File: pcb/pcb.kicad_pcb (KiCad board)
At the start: 2 copper layers, 54 parts, among them K00 Kailh Choc, K01 Kailh Choc, K02 Kailh Choc, K03 Kailh Choc, K10 Kailh Choc, K11 Kailh Choc, K12 Kailh Choc, K13 Kailh Choc, K20 Kailh Choc, K21 Kailh Choc, K22 Kailh Choc, K23 Kailh Choc, K30 Kailh Choc, K31 Kailh Choc, K32 Kailh Choc, K33 Kailh Choc, K40 Kailh Choc, K41 Kailh Choc, K42 Kailh Choc, K43 Kailh Choc, K50 Kailh Choc, K51 Kailh Choc, K52 Kailh Choc, K53 Kailh Choc, K60 Kailh Choc, K61 Kailh Choc, SW1 SW_DPST, U1 nice_nano

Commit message: first pass at pcb and case
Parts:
- removed D00, D01, D02, D03, D10, D11, D12, D13, D20, D21, D22, D23, D30, D31, D32, D33, D40, D41, D42, D43, D50, D51, D52, D53, D60, D61: 1N4148, Diode_THT:D_DO-35_SOD27_P7.62mm_Horizontal
- added J1: Screw_Terminal_01x02, Connector_JST:JST_PH_S2B-PH-K_1x02_P2.00mm_Horizontal, F.Cu at (189.5, 99.1)
- SW1: moved to B.Cu
- moved K13 336.6 mm to (90.8, 80.4), turned to 10.6 degrees
- moved K03 316.9 mm to (73.4, 85.4), turned to 10.6 degrees
- moved K00 304.1 mm to (82.8, 135.6), turned to 10.6 degrees
- moved K22 297.8 mm to (112.4, 88.3), turned to 8.36 degrees
- moved K33 294.9 mm to (131.7, 66.0), turned to 4.47 degrees
- moved K41 292.2 mm to (154.6, 100.4)
- moved K01 286.7 mm to (79.7, 118.8), turned to 10.6 degrees
- moved K10 286.6 mm to (100.2, 130.6), turned to 10.6 degrees
- moved K32 272.9 mm to (133.0, 83.0), turned to 4.47 degrees
- moved K11 269.7 mm to (97.1, 113.8), turned to 10.6 degrees
- moved K02 269.6 mm to (76.6, 102.1), turned to 10.6 degrees
- moved K43 257.2 mm to (154.6, 66.4)
- moved K51 254.7 mm to (172.6, 102.1)
- moved K12 253.1 mm to (93.9, 97.1), turned to 10.6 degrees
- moved K30 252.3 mm to (135.7, 116.9), turned to 4.47 degrees
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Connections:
- K00 pad 2: Net-(D00-Pad2) -> Row0
- K01 pad 2: Net-(D01-Pad2) -> Row1
- K02 pad 2: Net-(D02-Pad2) -> Row2
- K03 pad 2: Net-(D03-Pad2) -> Row3
- K10 pad 2: Net-(D10-Pad2) -> Row0
- K11 pad 2: Net-(D11-Pad2) -> Row1
- K12 pad 2: Net-(D12-Pad2) -> Row2
- K13 pad 2: Net-(D13-Pad2) -> Row3
- K20 pad 2: Net-(D20-Pad2) -> Row0
- K21 pad 2: Net-(D21-Pad2) -> Row1
- K22 pad 2: Net-(D22-Pad2) -> Row2
- K23 pad 2: Net-(D23-Pad2) -> Row3
- K30 pad 2: Net-(D30-Pad2) -> Row0
- K31 pad 2: Net-(D31-Pad2) -> Row1
- K32 pad 2: Net-(D32-Pad2) -> Row2
- K33 pad 2: Net-(D33-Pad2) -> Row3
- K40 pad 2: Net-(D40-Pad2) -> Row0
- K41 pad 2: Net-(D41-Pad2) -> Row1
- K42 pad 2: Net-(D42-Pad2) -> Row2
- K43 pad 2: Net-(D43-Pad2) -> Row3
- K50 pad 2: Net-(D50-Pad2) -> Row0
- K51 pad 2: Net-(D51-Pad2) -> Row1
- K52 pad 2: Net-(D52-Pad2) -> Row2
- K53 pad 2: Net-(D53-Pad2) -> Row3
- K60 pad 2: Net-(D60-Pad2) -> Row0
- K61 pad 2: Net-(D61-Pad2) -> Row1
- U1 pad 14: Col6 -> Col0
- U1 pad 15: Col5 -> Col2
- U1 pad 16: Col4 -> Col1
- U1 pad 18: Col2 -> Col4
- U1 pad 19: Col1 -> Col5
- U1 pad 20: Col0 -> Col6
- U1 pad 24: unconnected-(U1-Pad24) -> Net-(U1-Pad24)
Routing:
- net Col0: track 0.00 -> 211.6 mm, vias 0 -> 5
- net Col1: track 0.00 -> 194.2 mm, vias 0 -> 3
- net Row3: track 0.00 -> 189.7 mm, vias 0 -> 3
- net Row1: track 0.00 -> 181.7 mm, vias 0 -> 1
- net Row2: track 0.00 -> 168.0 mm, vias 0 -> 1
- net Col2: track 0.00 -> 167.6 mm, vias 0 -> 3
- net Row0: track 0.00 -> 155.7 mm, vias 0 -> 1
- net Col3: track 0.00 -> 148.4 mm, vias 0 -> 2
- net Col4: track 0.00 -> 130.7 mm, vias 0 -> 2
- net Col5: track 0.00 -> 121.7 mm, vias 0 -> 1
- net GND: track 0.00 -> 93.1 mm, vias 0 -> 3
- net Col6: track 0.00 -> 67.7 mm, vias 0 -> 3
- net Net-(U1-Pad24): track 0.00 -> 52.0 mm, vias 0 -> 1
- net Net-(SW1-Pad2): track 0.00 -> 27.1 mm, vias 0 -> 1
- net unconnected-(U1-Pad21): track 0.00 -> 21.3 mm, vias 0 -> 1
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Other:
- board outline added: 161.4 x 94.6 mm

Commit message: refining the shape
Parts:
- removed K61: Kailh Choc, lib:Kailh_socket_PG1350_reversible
- added JP1: SolderJumper_2_Open, Jumper:SolderJumper-2_P1.3mm_Open_TrianglePad1.0x1.5mm, F.Cu at (187.9, 64.8)
- added JP2: SolderJumper_2_Open, Jumper:SolderJumper-2_P1.3mm_Open_TrianglePad1.0x1.5mm, B.Cu at (188.0, 68.6)
- added JP3: SolderJumper_2_Open, Jumper:SolderJumper-2_P1.3mm_Open_TrianglePad1.0x1.5mm, B.Cu at (188.0, 64.8)
- added JP4: SolderJumper_2_Open, Jumper:SolderJumper-2_P1.3mm_Open_TrianglePad1.0x1.5mm, F.Cu at (188.0, 68.6)
- added SW2: SW_SPDT, lib:SW_SPDT_CK-JS102011SAQN, F.Cu at (196.3, 64.8)
- moved SW1 77.1 mm to (134.6, 98.4), turned to -175.53 degrees
- moved U1 35.1 mm to (188.4, 89.7), turned to 0 degrees
- moved J1 30.5 mm to (183.5, 69.2)
- moved K21 12.4 mm to (111.1, 93.3)
- moved K00 12.4 mm to (79.1, 123.7)
- moved K31 12.4 mm to (130.6, 88.1)
- moved K50 12.4 mm to (168.8, 107.3)
- moved K13 12.4 mm to (87.1, 68.5)
- moved K41 12.4 mm to (150.8, 88.6)
- moved K12 12.4 mm to (90.2, 85.3)
- moved K43 12.4 mm to (150.8, 54.5)
- moved K22 12.4 mm to (108.6, 76.5)
- moved K11 12.4 mm to (93.3, 102.0)
- moved K60 12.4 mm to (187.3, 120.4)
- moved K53 12.4 mm to (168.8, 56.3)
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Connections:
- J1 pad 1: Net-(U1-Pad24) -> Net-(J1-Pad1)
- J1 pad 2: GND -> Net-(J1-Pad2)
- SW1 pad 1: GND -> Net-(U1-Pad22)
- SW1 pad 2: Net-(SW1-Pad2) -> GND
- U1 pad 14: Col0 -> Col6
- U1 pad 15: Col2 -> Col0
- U1 pad 17: Col3 -> Col2
- U1 pad 18: Col4 -> Col3
- U1 pad 19: Col5 -> Col4
- U1 pad 20: Col6 -> Col5
- U1 pad 22: Net-(SW1-Pad2) -> Net-(U1-Pad22)
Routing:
- net Net-(U1-Pad22): track 0.00 -> 87.2 mm, vias 0 -> 3
- net Row1: track 181.7 -> 140.9 mm
- net Net-(U1-Pad24): track 52.0 -> 22.4 mm, vias 1 -> 2
- net GND: track 93.1 -> 122.4 mm, vias 3 -> 7
- net Col0: track 211.6 -> 183.9 mm, vias 5 -> 1
- net Col6: track 67.7 -> 40.0 mm, vias 3 -> 1
- net Net-(SW1-Pad2): track 27.1 -> 0.00 mm, vias 1 -> 0
- net Col1: track 194.2 -> 168.4 mm, vias 3 -> 1
- net Col5: track 121.7 -> 101.4 mm
- net Net-(J1-Pad2): track 0.00 -> 15.8 mm
- net unconnected-(U1-Pad21): track 21.3 -> 8.25 mm
- net Col2: track 167.6 -> 155.1 mm, vias 3 -> 1
- net Row0: track 155.7 -> 143.7 mm
- net Net-(SW2-Pad2): track 0.00 -> 10.4 mm, vias 0 -> 1
- net Net-(J1-Pad1): track 0.00 -> 9.64 mm
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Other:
- board size 161.4 x 94.6 mm -> 139.7 x 86.5 mm
- board text added: "C0,1 =10.6deg"
- board text added: "C2 = 8.36deg"
- board text added: "C3 = 4.47deg"
- board text added: "Solder jumpers on OPPOSITE side that mcu is mounted"

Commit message: playing around with layouts & shapes
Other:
- board size 139.7 x 86.5 mm -> 140 x 86.7 mm

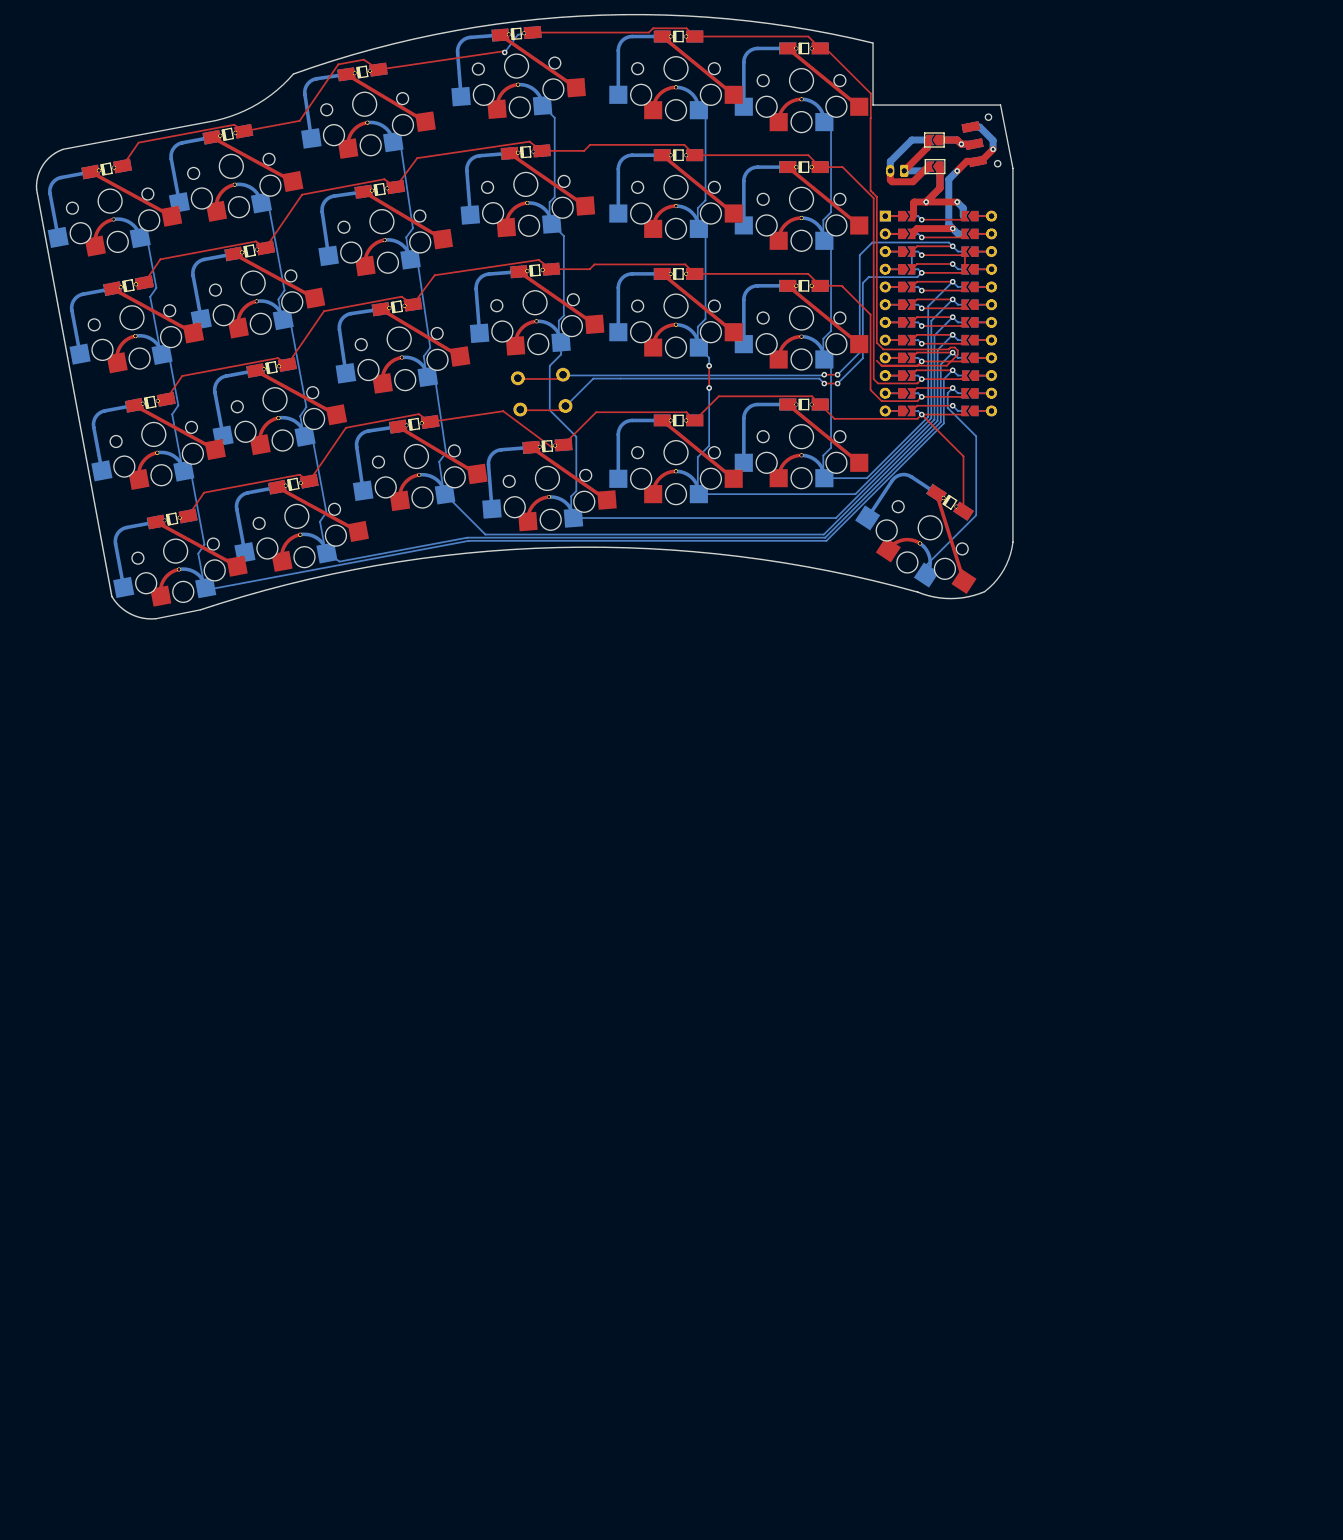
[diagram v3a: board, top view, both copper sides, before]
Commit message: update pcb for new shape
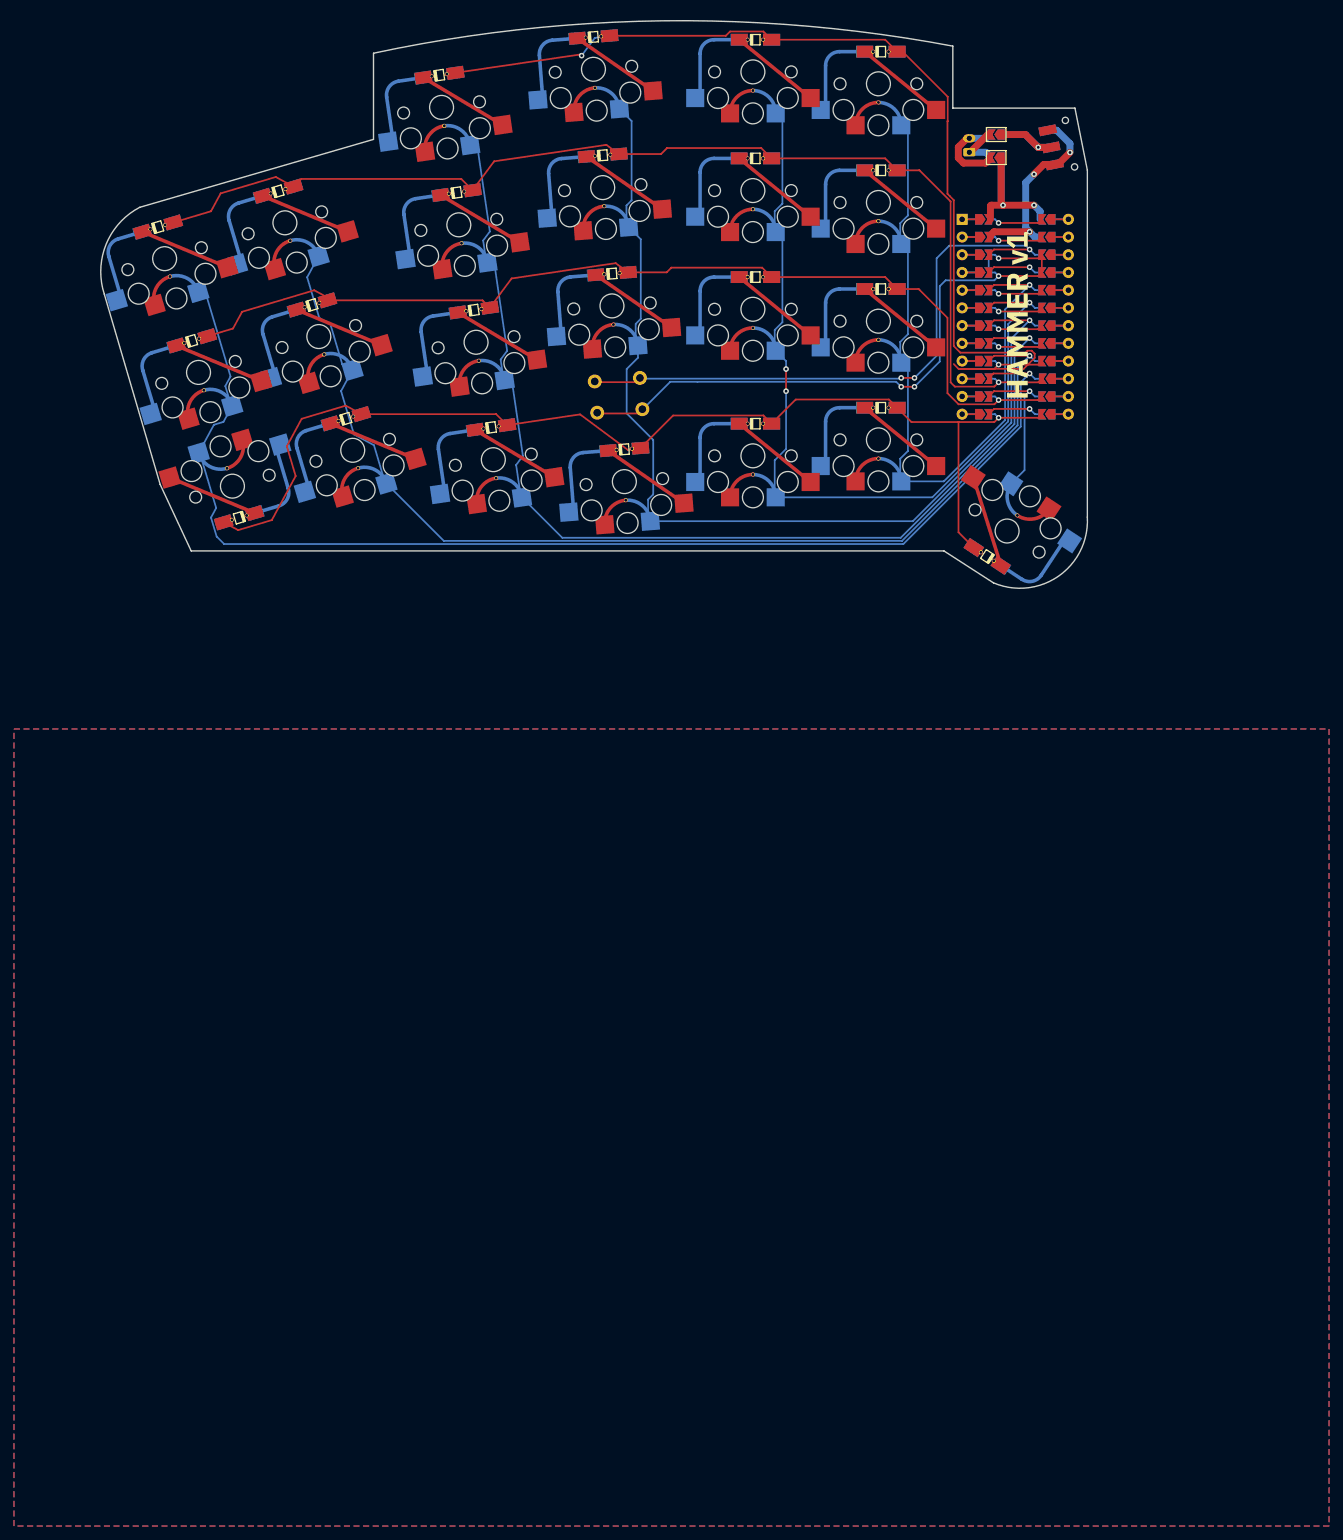
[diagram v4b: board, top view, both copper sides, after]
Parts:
- removed K03, K13: Kailh Choc, lib:Kailh_socket_PG1350_reversible
- moved K10 12.4 mm to (104.5, 109.3), turned to 16.6 degrees
- moved K00 12.4 mm to (87.2, 114.4), turned to -163.4 degrees
- moved K22 11.0 mm to (119.7, 76.9)
- moved K30 11.0 mm to (143.4, 113.8)
- moved K32 11.0 mm to (140.3, 71.6)
- moved K41 11.0 mm to (161.8, 89.0)
- moved K42 11.0 mm to (161.8, 72.0)
- moved SW1 11.0 mm to (145.6, 98.9)
- moved SW2 11.0 mm to (207.3, 65.3)
- moved K21 11.0 mm to (122.1, 93.8)
- moved K52 11.0 mm to (179.8, 73.7)
- moved K53 11.0 mm to (179.8, 56.7)
- moved K51 11.0 mm to (179.8, 90.7)
- moved K20 11.0 mm to (124.6, 110.6)
- moved K40 11.0 mm to (161.8, 110.1)
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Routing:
- net Row3: track 195.8 -> 151.9 mm
- net Col6: track 40.0 -> 22.6 mm
- net Row0: track 143.7 -> 158.9 mm
- net Col1: track 168.4 -> 157.8 mm
- net Net-(SW2-Pad2): track 10.4 -> 15.8 mm
- net Col0: track 183.9 -> 178.6 mm
- net Net-(J1-Pad2): track 15.8 -> 12.0 mm
- net Row2: track 159.1 -> 162.7 mm
- net Net-(J1-Pad1): track 9.64 -> 7.28 mm
- net Net-(U1-Pad24): track 22.4 -> 24.5 mm
- net Row1: track 140.9 -> 142.3 mm
- added copper zone on B.Cu, net GND
- added copper zone on F.Cu, net GND
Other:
- board size 140 x 86.7 mm -> 141.5 x 81.4 mm
- board text added: "C0,1 =16.6deg"
- board text added: "Solder jumpers on OPPOSITE side that component is mounted"
- board text added: "thumb = 33.4deg"
- board text removed: "C0,1 =10.6deg"
- board text removed: "Solder jumpers on OPPOSITE side that mcu is mounted"

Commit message: update pcb
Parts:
- added SW3: SW_Push_DPDT, lib:SW_JS202011SCQN (Reverse Mount), B.Cu at (203.8, 67.9)
- SW2: value SW_SPDT -> SW_Push_DPDT; footprint lib:SW_SPDT_CK-JS102011SAQN -> lib:SW_JS202011SCQN (Reverse Mount)
- moved J1 4.73 mm to (196.1, 70.0), turned to 180 degrees
- moved SW2 4.38 mm to (203.8, 67.9), turned to -90 degrees
- moved JP2 3.30 mm to (193.7, 66.0), turned to -90 degrees
- moved JP4 3.30 mm to (193.7, 66.0), turned to -90 degrees
- moved JP1 2.06 mm to (196.8, 66.0), turned to -90 degrees
- moved JP3 2.06 mm to (196.8, 66.0), turned to -90 degrees
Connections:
- JP1 pad 1: Net-(SW2-Pad2) -> Net-(JP1-Pad1)
- JP2 pad 1: Net-(U1-Pad24) -> Net-(JP2-Pad1)
- JP3 pad 1: Net-(SW2-Pad2) -> Net-(JP1-Pad1)
- JP4 pad 1: Net-(U1-Pad24) -> Net-(JP2-Pad1)
- SW2 pad 1: GND -> unconnected-(SW2-Pad1)
- SW2 pad 2: Net-(SW2-Pad2) -> Net-(JP2-Pad1)
- SW2 pad 3: unconnected-(SW2-Pad3) -> Net-(U1-Pad24)
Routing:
- net Net-(JP2-Pad1): track 0.00 -> 29.0 mm, vias 0 -> 2
- net Row3: track 151.9 -> 130.0 mm
- net GND: track 122.4 -> 105.5 mm, vias 7 -> 5
- net Net-(SW2-Pad2): track 15.8 -> 0.00 mm, vias 1 -> 0
- net Net-(JP1-Pad1): track 0.00 -> 9.86 mm
- net Net-(U1-Pad24): track 24.5 -> 21.1 mm
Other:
- outline, holes or cut-outs redrawn

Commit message: switch to low-profile battery connector
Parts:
- removed JP1, JP2, JP3, JP4: SolderJumper_2_Open, Jumper:SolderJumper-2_P1.3mm_Open_TrianglePad1.0x1.5mm
- added J2: Screw_Terminal_01x02, lib:BM02B-ACHSS-GAN-ETF, B.Cu at (194.3, 64.8)
- J1: footprint Connector_JST:JST_PH_S2B-PH-K_1x02_P2.00mm_Horizontal -> lib:BM02B-ACHSS-GAN-ETF
- moved J1 5.53 mm to (194.3, 64.8), turned to -90 degrees
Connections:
- SW2 pad 2: Net-(JP2-Pad1) -> Net-(J1-Pad2)
- SW2 pad 5: Net-(JP1-Pad1) -> Net-(J1-Pad1)
- SW3 pad 2: Net-(JP2-Pad1) -> Net-(SW3-Pad2)
- SW3 pad 5: Net-(JP1-Pad1) -> Net-(SW3-Pad5)
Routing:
- net Net-(JP2-Pad1): track 29.0 -> 0.00 mm, vias 2 -> 0
- net Net-(SW3-Pad2): track 0.00 -> 23.1 mm
- net Net-(JP1-Pad1): track 9.86 -> 0.00 mm
- net Net-(J1-Pad2): track 12.1 -> 20.9 mm
- net Net-(SW3-Pad5): track 0.00 -> 6.14 mm
- net Net-(J1-Pad1): track 7.61 -> 9.70 mm
